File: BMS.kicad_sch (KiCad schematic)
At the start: 52 parts, among them J28 OLED, SW13 SW_DIP_x01, U1 TSR_1-2433, U2 TSR_1-2450, U4 Teensy4.1, U6 MCP2562-E-SN

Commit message: Added isolated CAN, UART and PWR
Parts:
- removed JP11: SolderJumper_2_Open, Jumper:SolderJumper-2_P1.3mm_Open_RoundedPad1.0x1.5mm, symbol Jumper:SolderJumper_2_Open
- removed R21, R22, R23, R24, R25, R26, R27, R28, R29, R30, R31, R32, R33, R34, R35, R36, R37, R42, R43, R44, R45, R46, R47, R48, R49, R50, R51, R54, R55, R59: 330R, Resistor_SMD:R_0603_1608Metric, symbol Device:R
- removed U1: TSR_1-2433, Converter_DCDC:Converter_DCDC_TRACO_TSR-1_THT, symbol Regulator_Switching:TSR_1-2433
- removed U6: MCP2562-E-SN, Package_SO:SOIC-8_3.9x4.9mm_P1.27mm, symbol Interface_CAN_LIN:MCP2562-E-SN
- added C6, C7: 1uF, Capacitor_SMD:C_0603_1608Metric, symbol Device:C
- added U3: ISO1050DUB, Package_SO:SOP-8_6.62x9.15mm_P2.54mm, symbol Interface_CAN_LIN:ISO1050DUB
- added U5: ISO7221C, Package_SO:SOIC-8_3.9x4.9mm_P1.27mm, symbol Isolator:ISO7321C
- added U6: TBA1-0511E, Converter_DCDC:Converter_DCDC_TRACO_TBA1-xxxxE_Single_THT, symbol Converter_DCDC:TBA1-0511E
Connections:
- net D1_D is gone; now on an unnamed net: R40.2
- net +3.3V: now also U4.46 (3V3), C6.1, U3.1 (VCC1), U5.1 (VCC1)
- net +5V: now also U6.1 (+Vin); no longer C5.1
- net GND: now also C6.2, C7.2, U3.4 (GND1), U5.4 (GND1), U6.2 (-Vin)
- net I2C_SCL: no longer U4.41 (19_A5_SCL)
- net I2C_SDA: no longer U4.40 (18_A4_SDA)
- net at U4.20 (28_RX7): no longer R41.2
- net at U4.21 (29_TX7): no longer R40.1
- net at U4.45 (23_A9_CRX1_MCLK1): now also R41.2
- net CAN_HIGH renamed CAN_HIGH_ISO
- net CAN_HIGH_ISO: now also U3.7 (CANH)
- net CAN_LOW renamed CAN_LOW_ISO
- net CAN_LOW_ISO: now also U3.6 (CANL)
- net D4_C renamed CAN1_RX
- net CAN1_RX: now also U3.2 (RXD)
- net Teensy_CAN_RX: no longer names the net of R39.2
- net Teensy_CAN_TX: no longer names the net of R38.2
- net V_Supply_SD4se renamed V_Supply_Sense
- new net +5V_ISO: C5.1, C7.1, U3.8 (VCC2), U5.8 (VCC2), U6.6 (+Vout)
- new net CAN1_TX: R40.1, U3.3 (TXD)
- new net GND_ISO: U3.5 (GND2), U5.5 (GND2), U6.4 (-Vout)
- new net UART_RX: U5.2 (OUTA)
- new net UART_RX_ISO: U5.7 (INA)
- new net UART_TX: U5.3 (INB)
- new net UART_TX_ISO: U5.6 (OUTB)
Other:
- note added: "Isolated CAN Transceiver Circuit"
- note added: "Isolated UART Interface"
- note added: "NOT on LCSC"
- note removed: "Transceiver Circuit"
- moved on the sheet: C4, C5, JP12, R39, R52, R53, R6, SW13, TP1, TP2, TP3, U4

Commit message: Adding BOM Info
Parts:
- removed C4, C5, C6, C7: 1uF, Capacitor_SMD:C_0603_1608Metric, symbol Device:C
- removed JP12: SolderJumper_2_Open, Jumper:SolderJumper-2_P1.3mm_Open_RoundedPad1.0x1.5mm, symbol Jumper:SolderJumper_2_Open
- removed R38, R39, R40, R41, R52, R53: 330R, Resistor_SMD:R_0603_1608Metric, symbol Device:R
- removed R6: 120, Resistor_SMD:R_0603_1608Metric, symbol Device:R
- removed SW13: SW_DIP_x01, Button_Switch_SMD:SW_DIP_SPSTx01_Slide_Copal_CHS-01B_W7.62mm_P1.27mm, symbol Switch:SW_DIP_x01
- removed U3: ISO1050DUB, Package_SO:SOP-8_6.62x9.15mm_P2.54mm, symbol Interface_CAN_LIN:ISO1050DUB
- removed U5: ISO7221C, Package_SO:SOIC-8_3.9x4.9mm_P1.27mm, symbol Isolator:ISO7321C
- added BT1: Battery_Cell, symbol Device:Battery_Cell
- added BZ1: Buzzer, Buzzer_Beeper:Buzzer_12x9.5RM7.6, symbol Device:Buzzer
- added C2: 470uF, Capacitor_SMD:CP_Elec_10x10, symbol Device:C_Polarized
- added D1: LED, LED_SMD:LED_0603_1608Metric, symbol Device:LED
- added L1: 1.5uH, Inductor_SMD:L_Changjiang_FXL0618, symbol Device:L
- added R1: 10k, Resistor_SMD:R_0805_2012Metric, symbol Device:R
- added TP1, TP3, TP4: TestPoint, TestPoint:TestPoint_Pad_2.5x2.5mm, symbol Connector:TestPoint
- C1: value 1000uf 50V -> 470uF; footprint Capacitor_THT:CP_Radial_D10.0mm_P5.00mm_P7.50mm -> Capacitor_SMD:CP_Elec_10x10; LCSC C88721 -> C178579
- F1: value 20A Fuse -> Mini Blade Fuse (10A); footprint Fuse:Fuseholder_Blade_ATO_Littelfuse_Pudenz_2_Pin -> user:XFCN XF-508P-B-B; LCSC (none) -> C19727305; MPN (none) -> XF-508P-B-B; Manufacturer (none) -> XFCN
- U1: renamed from U2; value TSR_1-2450 -> TSR_1-3450
- U2: renamed from U6; value TBA1-0511E -> B0505S-3WR2; LCSC (none) -> C5369498; MPN (none) -> B0505S-3WR2; Manufacturer (none) -> YLPTEC
- U3: renamed from U4; footprint teensy:Teensy41 -> teensy_library:Teensy_4.1_RTC
- renumbered J28 to J1, TP1 to TP2, TP2 to TP5, TP3 to TP6
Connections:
- net +5V_ISO is gone; now on net +5V: U2.6 (+Vout)
- net GND_ISO is gone; now on net GND: U2.4 (-Vout)
- net +12V: now also C2.1, L1.2; no longer C1.1, F1.2
- net +3.3V: now also U3.15 (3V3), U3.50 (3.3V)
- net +5V: now also TP3.1
- net CAN1_RX: now also U3.45 (23_A9_CRX1_MCLK1)
- net CAN1_TX: now also U3.44 (22_A8_CTX1)
- net GND: now also U3.51 (GND), BT1.2 (-), C2.2, TP1.1, TP4.1
- net RAW_INPUT: now also BZ1.1 (+), R1.2
- net SERIAL_TX: now reaches U3.10 (8_TX2_IN1)
- net CAN2_RX: now reaches U3.2 (0_RX1_CRX2_CS1)
- net CAN3_RX: now reaches U3.22 (30_CRX3)
- net CAN3_TX: now reaches U3.23 (31_CTX3)
- net CAN2_TX: now reaches U3.3 (1_TX1_CTX2_MISO1)
- net SERIAL_RX: now reaches U3.9 (7_RX2_OUT1A)
- new net: BZ1.2 (-), C1.1, D1.1 (K), F1.2, L1.1
- new net: D1.2 (A), R1.1
- new net RTC_BATT_+: BT1.1 (+), U3.49 (V_BATT_RTC)
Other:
- added sheet CAN Transceiver (CAN_Transceiver.kicad_sch)
- added sheet CAN Transceiver1 (CAN_Transceiver.kicad_sch)
- added sheet CAN_1 (Isolated_CAN_Transceiver.kicad_sch)
- added sheet UART_1 (UARTlated_Interface.kicad_sch)
- note added: "3.3v Out from Teesny"
- note added: "CAN Transceivers - Non Isolated"
- note added: "CAN1 ISOLATED"
- note added: "LPF Pi Filter 10A F_{c}=87.6Hz"
- note added: "RTC Battery"
- note added: "Serial ISOLATED"
- note removed: "Isolated CAN Transceiver Circuit"
- note removed: "Isolated UART Interface"
- note removed: "NOT on LCSC"
- moved on the sheet: F1, TP2, TP5, TP6, U1, U2

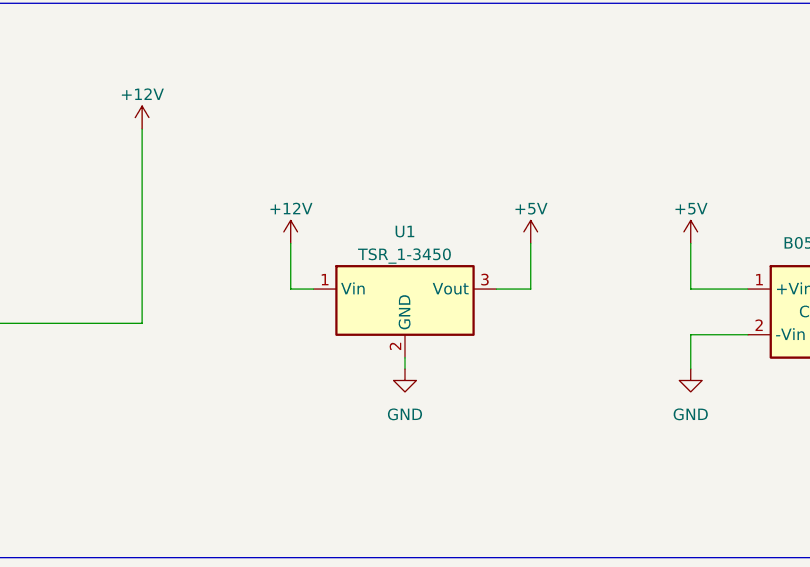
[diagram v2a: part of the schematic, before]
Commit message: Adding Part Numbers
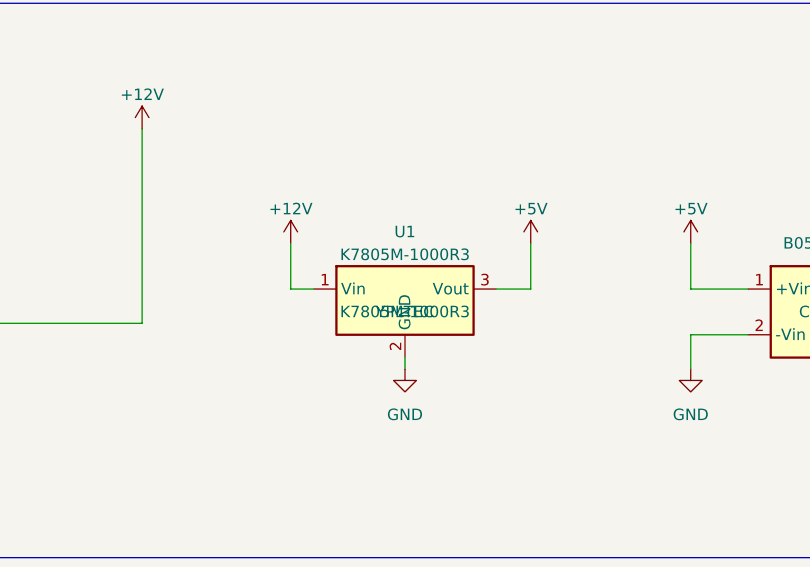
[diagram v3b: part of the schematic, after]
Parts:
- U1: value TSR_1-3450 -> K7805M-1000R3; LCSC C132362 -> C5369649; MPN (none) -> K7805M-1000R3; Manufacturer (none) -> YPLTEC
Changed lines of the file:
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@@
 			)
 		)
-		(property "Value" "TSR_1-3450"
+		(property "Value" "K7805M-1000R3"
 			(at 361.95 48.26 0)
 			(effects
@@
 			)
 		)
-		(property "Datasheet" "http://www.tracopower.com/products/tsr1.pdf"
+		(property "Datasheet" "https://www.lcsc.com/datasheet/lcsc_datasheet_2306121442_YLPTEC-K7805M-1000R3_C5369649.pdf"
 			(at 361.95 54.61 0)
 			(effects
@@
 			)
 		)
-		(property "LCSC" "C132362"
+		(property "LCSC" "C5369649"
 			(at 361.95 54.61 0)
 			(effects
@@
 			)
 		)
+		(property "MPN" "K7805M-1000R3"
+			(at 361.95 54.61 0)
+			(effects
+				(font
+					(size 1.27 1.27)
+				)
+			)
+		)
+		(property "Manufacturer" "YPLTEC"
+			(at 361.95 54.61 0)
+			(effects
+				(font
+					(size 1.27 1.27)
+				)
+			)
+		)

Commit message: Connectors, high side circuits added, layout progressed
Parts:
- added D21: 10V, Diode_SMD:D_SOD-123, symbol Device:D_Zener
- added J1, J2, J6: Conn_02x02_Counter_Clockwise, Connector_Molex:Molex_Mini-Fit_Jr_5566-04A_2x02_P4.20mm_Vertical, symbol Connector_Generic:Conn_02x02_Counter_Clockwise
- added J3: RJ45, Connector_RJ:RJ45_Molex_0855135013_Vertical, symbol Connector:RJ45
- added J4: Conn_02x08_Top_Bottom, Connector_Molex:Molex_Mini-Fit_Jr_5566-16A_2x08_P4.20mm_Vertical, symbol Connector_Generic:Conn_02x08_Top_Bottom
- added J5: Conn_02x05_Top_Bottom, Connector_Molex:Molex_Mini-Fit_Jr_5566-10A_2x05_P4.20mm_Vertical, symbol Connector_Generic:Conn_02x05_Top_Bottom
- added Q2: SIRA00DP-T1-GE3, Package_SO:PowerPAK_SO-8_Single, symbol Transistor_FET:IRLZ34N
- added R28: 10k, Resistor_SMD:R_0805_2012Metric, symbol Device:R
- BT1: footprint (none) -> Battery:BatteryHolder_Keystone_1060_1x2032
- renumbered J1 to J10
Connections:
- net +12V: now also D21.1 (K), J3.2, J3.4, J4.10 (Pin_10), J4.11 (Pin_11), J4.9 (Pin_9), Q2.5 (D); no longer C2.1, L1.2
- net +5V: no longer TP3.1, U2.6 (+Vout)
- net CAN2_HIGH: now also J5.4 (Pin_4)
- net CAN2_LOW: now also J5.9 (Pin_9)
- net CAN3_HIGH: now also J3.7
- net CAN3_LOW: now also J3.8
- net GND: now also J2.1 (Pin_1), J3.1, J3.5, J4.16 (Pin_16), J4.2 (Pin_2), J4.3 (Pin_3), J5.10 (Pin_10), R28.1; no longer TP1.1, U2.4 (-Vout)
- net HSD_Positive_Contactor_LOGIC: now reaches U3.13 (11_MOSI_CTX1)
- net HSD_PreCharge_Contactor_LOGIC: now reaches U3.14 (12_MISO_MQSL)
- net HSD_Charge_Contactor_LOGIC: now reaches U3.42 (20_A6_TX5_LRCLK1)
- net HSD_Negative_Contactor_LOGIC: now reaches U3.43 (21_A7_RX5_BCLK1)
- net RAW_INPUT renamed 12V_INPUT
- net 12V_INPUT: now also J4.8 (Pin_8)
- new net: C2.1, L1.2, Q2.1 (S), Q2.2 (S), Q2.3 (S)
- new net: D21.2 (A), Q2.4 (G), R28.2
- new net +5V_ISO: TP3.1, U2.6 (+Vout)
- new net CAN1_HIGH_ISO: J6.1 (Pin_1), J6.3 (Pin_3)
- new net CAN1_LOW_ISO: J6.2 (Pin_2), J6.4 (Pin_4)
- new net Current_Sense_In_High: J2.4 (Pin_4)
- new net Current_Sense_In_Low: J2.3 (Pin_3)
- new net GND_ISO: J1.1 (Pin_1), TP1.1, U2.4 (-Vout)
- new net In_1: J5.1 (Pin_1)
- new net In_2: J5.2 (Pin_2)
- new net In_3: J5.6 (Pin_6)
- new net In_4: J5.7 (Pin_7)
- new net OUT1_HSD_PWR: J4.12 (Pin_12)
- new net OUT2_HSD_PWR: J4.4 (Pin_4)
- new net OUT3_HSD_PWR: J4.13 (Pin_13)
- new net OUT4_HSD_PWR: J4.5 (Pin_5)
- new net OUT5_LSD_PWR: J4.14 (Pin_14)
- new net OUT6_LSD_PWR: J4.6 (Pin_6)
- new net OUT7_LSD_PWR: J4.7 (Pin_7)
- new net OUT8_LSD_PWR: J4.15 (Pin_15)
- new net Overcurrent_Protection/V_{OUT}: J5.5 (Pin_5)
- new net Overcurrent_Protection1/V_{OUT}: J4.1 (Pin_1)
- new net Overcurrent_Protection2/V_{OUT}: J2.2 (Pin_2)
- new net Overcurrent_Protection3/V_{OUT}: J1.2 (Pin_2)
- new net RX_2: J5.8 (Pin_8)
- new net TX_2: J5.3 (Pin_3)
- new net UART_RX_ISO: J1.3 (Pin_3)
- new net UART_TX_ISO: J1.4 (Pin_4)
- no-connect marks 1 -> 0
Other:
- sheet CAN_1 renamed Isolated_CAN_1
- sheet UART_1 renamed Isolated_UART
- added sheet High Side Drivers (4_High_Side_Driver.kicad_sch)
- added sheet Overcurrent_Protection (5V_Overcurrent_Protection.kicad_sch)
- added sheet Overcurrent_Protection1 (5V_Overcurrent_Protection.kicad_sch)
- added sheet Overcurrent_Protection2 (5V_Overcurrent_Protection.kicad_sch)
- added sheet Overcurrent_Protection3 (5V_Overcurrent_Protection.kicad_sch)
- sheet Isolated_CAN_1 ports: added ISO_GND; removed GND
- sheet Isolated_UART: file UARTlated_Interface.kicad_sch -> UART_Isolated_Interface.kicad_sch
- sheet Isolated_UART ports: added ISO_GND; removed GND
- note added: "Test Points ISO"
- moved on the sheet: C1, C2, L1, TP1, TP3, TP4, TP6

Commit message: Added LSD, HSD, Improved Layout
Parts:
- added C11, C12: 1uF, Capacitor_SMD:C_0603_1608Metric, symbol Device:C
- added D22, D27, D28, D29: 4.7V Zener 500mW, Diode_SMD:D_SOD-123, symbol Device:D_Zener
- added R29, R34, R35, R36: 4.7k, Resistor_SMD:R_0603_1608Metric, symbol Device:R
- added U14: CA-IS3740, Package_SO:SOIC-16W_7.5x10.3mm_P1.27mm, symbol User:CA-IS3740HB
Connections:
- net +3.3V: now also C12.2, U14.16 (VDD_{B})
- net +5V: now also C11.1, U14.1 (VDD_{A})
- net GND: now also C11.2, C12.1, D22.2 (A), D27.2 (A), D28.2 (A), D29.2 (A), U14.10 (EN_{B}), U14.15 (GND_{B}), U14.2 (GND_{A}), U14.7 (EN_{A}), U14.8 (GND_{A}), U14.9 (GND_{B})
- net In_1: now also R29.1
- net In_2: now also R34.1
- net In_3: now also R35.1
- net In_4: now also R36.1
- net OUT5_LSD_LOGIC: now reaches U3.4 (2_OUT2)
- net OUT6_LSD_LOGIC: now reaches U3.5 (3_LRCLK2)
- net OUT7_LSD_LOGIC: now reaches U3.7 (5_IN2)
- net OUT8_LSD_LOGIC: now reaches U3.8 (6_OUT1D)
- net HSD_Charge_Contactor_LOGIC renamed OUT3_HSD_LOGIC
- net HSD_Negative_Contactor_LOGIC renamed OUT4_HSD_LOGIC
- net HSD_Positive_Contactor_LOGIC renamed OUT1_HSD_LOGIC
- net HSD_PreCharge_Contactor_LOGIC renamed OUT2_HSD_LOGIC
- new net: D28.1 (K), R35.2, U14.5 (In_{3})
- new net: D22.1 (K), R29.2, U14.3 (In_{1})
- new net: D27.1 (K), R34.2, U14.4 (In_{2})
- new net: D29.1 (K), R36.2, U14.6 (In_{4})
- new net Logic_IN_1: U14.14 (Out_{1})
- new net Logic_IN_2: U14.13 (Out_{2})
- new net Logic_IN_3: U14.12 (Out_{3})
- new net Logic_IN_4: U14.11 (Out_{4})
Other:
- added sheet Low Side Drivers (4 High Current Low Side Drivers.kicad_sch)
- note added: "High Side Drivers"
- note added: "Isolated Digital Inputs"
- note added: "Low Side Drivers"

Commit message: Added 12v Out Protection, generally completed layout
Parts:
- added C13: 470uF, Capacitor_SMD:CP_Elec_10x10, symbol Device:C_Polarized
- added C14: 1uF, Capacitor_SMD:C_0603_1608Metric, symbol Device:C
- TP1, TP4: footprint TestPoint:TestPoint_Pad_2.5x2.5mm -> user:Clip_TP
- TP2, TP3, TP5, TP6: footprint TestPoint:TestPoint_Pad_2.5x2.5mm -> user:STD_TP
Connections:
- net +12V: no longer J4.10 (Pin_10), J4.11 (Pin_11), J4.9 (Pin_9)
- net GND_ISO: now also C13.2, C14.2
- net Logic_IN_1: now also U3.38 (16_A2_RX4_SCL1)
- net Logic_IN_2: now also U3.39 (17_A3_TX4_SDA1)
- net Logic_IN_3: now also U3.40 (18_A4_SDA)
- net Logic_IN_4: now also U3.41 (19_A5_SCL)
- net Overcurrent_Protection3/V_{OUT}: now also C13.1, C14.1
- net OUT5_LSD_Status: now reaches U3.17 (25_A11_RX6_SDA2)
- net OUT6_LSD_Status: now reaches U3.18 (26_A12_MOSI1)
- net OUT7_LSD_Status: now reaches U3.19 (27_A13_SCK1)
- net OUT8_LSD_Status: now reaches U3.20 (28_RX7)
- new net 12V_Out_Bank1: J4.9 (Pin_9)
- new net 12V_Out_Bank2: J4.10 (Pin_10), J4.11 (Pin_11)
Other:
- removed sheet Low Side Drivers
- added sheet 12V_Output_Protection (12V_Output_Protection.kicad_sch)
- added sheet 4 Smart Low Side Driver (4_Smart_LSD.kicad_sch)

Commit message: All the diodes, and other layout work
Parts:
- added D31, D32: D, Diode_SMD:D_SOD-123, symbol Device:D
- added Q1: BSS138LT1G, Package_TO_SOT_SMD:SOT-23, symbol Transistor_FET_Other:Q_NMOS_Depletion_GSD
- added R53: 4.7k, Resistor_SMD:R_0603_1608Metric, symbol Device:R
- added R54: 330, Resistor_SMD:R_0603_1608Metric, symbol Device:R
- Q2: value SIRA00DP-T1-GE3 -> HSBA100P03; LCSC C141540 -> C701057
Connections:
- net V_Supply_Sense is gone; now on net I2C_SCL: U3.16 (24_A10_TX6_SCL2)
- net +12V: now also Q2.6 (D), Q2.7 (D), Q2.8 (D), D31.1 (K)
- net GND: now also Q1.2 (S), R53.2
- net I2C_SDA: now also U3.17 (25_A11_RX6_SDA2)
- net OUT5_LSD_Status: now also U3.18 (26_A12_MOSI1); no longer U3.17 (25_A11_RX6_SDA2)
- net OUT6_LSD_Status: now also U3.19 (27_A13_SCK1); no longer U3.18 (26_A12_MOSI1)
- net OUT7_LSD_Status: now also U3.20 (28_RX7); no longer U3.19 (27_A13_SCK1)
- net OUT8_LSD_Status: now also U3.21 (29_TX7); no longer U3.20 (28_RX7)
- net at C1.1, D1.1 (K), F1.2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: no longer BZ1.2 (-)
- net Buzzer_Logic: now reaches U3.12 (10_CS_MQSR)
- net Buzzer_Logic: now also R54.2
- new net: BZ1.2 (-), D31.2 (A), D32.2 (A)
- new net: Q1.1 (G), R53.1, R54.1
- new net Buzzer_-ve: D32.1 (K), Q1.3 (D)
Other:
- sheet 4 Smart Low Side Driver ports: added V_{logic}; removed Logic_V
- note added: "Buzzer Driver"
- moved on the sheet: BZ1

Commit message: Layout, smaller resistors and HB + Error LEDs
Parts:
- added D41: LED, LED_SMD:LED_1206_3216Metric, symbol Device:LED
- added D42: LED, LED_SMD:LED_0603_1608Metric, symbol Device:LED
- added J7: Conn_02x02_Counter_Clockwise, Connector_Molex:Molex_Mini-Fit_Jr_5566-04A_2x02_P4.20mm_Vertical, symbol Connector_Generic:Conn_02x02_Counter_Clockwise
- added Q3, Q4: BSS138LT1G, Package_TO_SOT_SMD:SOT-23, symbol Transistor_FET_Other:Q_NMOS_Depletion_GSD
- added R55, R60: 1k, Resistor_SMD:R_0603_1608Metric, symbol Device:R
- added R56, R59: 47k, Resistor_SMD:R_0603_1608Metric, symbol Device:R
- added R57: 330, Resistor_SMD:R_0603_1608Metric, symbol Device:R
- added R58: 1K, Resistor_SMD:R_0603_1608Metric, symbol Device:R
- D31, D32: footprint Diode_SMD:D_SOD-123 -> Diode_SMD:D_SOD-523; LCSC C83152 -> C139439; MPN BAT46W-7-F -> SDM20U40-7
- J1, J2, J6: LCSC (none) -> C2845777
- J4: LCSC (none) -> C2845783
- J5: LCSC (none) -> C2845780
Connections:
- net +5V: now also R57.1, R60.1
- net GND: now also Q3.2 (S), Q4.2 (S), R56.2, R59.2
- net ERROR_LED: now reaches U3.24 (32_OUT1B)
- net ERROR_LED: now also R55.2
- net HSD_SEL_0_A: now reaches U3.25 (33_MCLK2)
- net HSD_SEL_1_A: now reaches U3.26 (34_RX8)
- net HSD_SEn_A: now reaches U3.27 (35_TX8)
- net HSD_MULTISENSE_A: now reaches U3.28 (36_CS)
- net HSD_SEL_0_B: now reaches U3.29 (37_CS)
- net HSD_SEL_1_B: now reaches U3.30 (38_CS1_IN1)
- net HSD_SEn_B: now reaches U3.31 (39_MISO1_OUT1A)
- net HSD_MULTISENSE_B: now reaches U3.32 (40_A16)
- net HSD_FAULT_RESET: now reaches U3.33 (41_A17)
- net HEARTBEAT_LED: now reaches U3.6 (4_BCLK2)
- net HEARTBEAT_LED: now also R58.2
- new net: Q3.1 (G), R55.1, R56.1
- new net: D41.1 (K), Q3.3 (D)
- new net: D41.2 (A), R57.2
- new net: Q4.1 (G), R58.1, R59.1
- new net: D42.1 (K), Q4.3 (D)
- new net: D42.2 (A), R60.2
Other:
- note added: "Active LEDs"
- moved on the sheet: TP2, TP4, TP5, TP6
